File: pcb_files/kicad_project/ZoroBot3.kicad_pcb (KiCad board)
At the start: 2 copper layers, 85.8 x 91.9 mm, 197 parts, among them Q1 NMOS, Q2 AON7423, Q3 ST-1KL3A, Q4 ST-1KL3A, Q5 ST-1KL3A, Q6 ST-1KL3A, U1 MPU-6500, U2 MPU-6500, Y1 Crystal_GND24

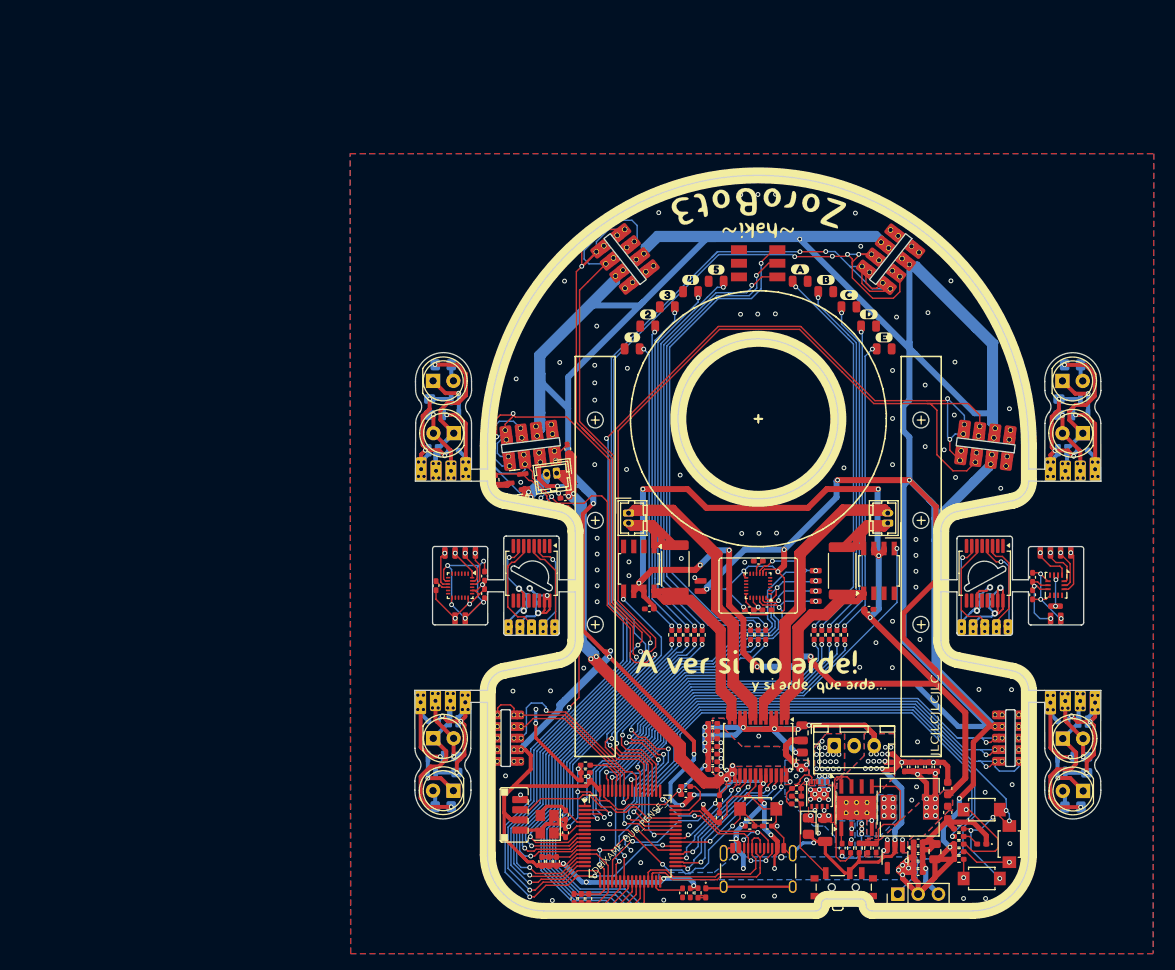
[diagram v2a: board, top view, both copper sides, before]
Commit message: Cambia el puente H al MP6551
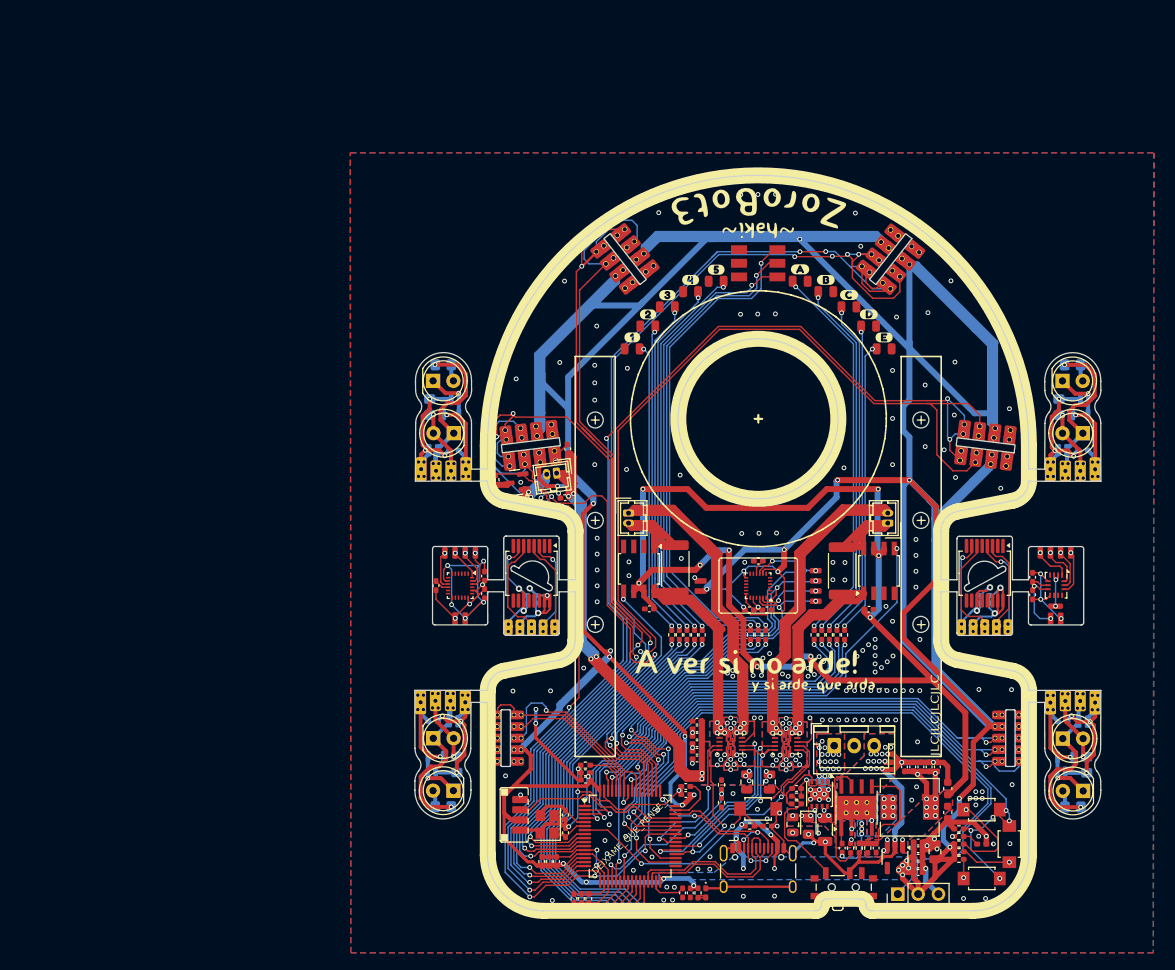
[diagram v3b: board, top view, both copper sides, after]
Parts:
- added PH2: ~, custom_footprints:PH-MP6551GQB-P, F.Cu at (147.1, 122.2)
- C43: footprint Capacitor_SMD:C_0402_1005Metric_Pad0.74x0.62mm_HandSolder -> Capacitor_SMD:C_0805_2012Metric
- PH1: footprint Package_SO:SSOP-24_5.3x8.2mm_P0.65mm -> custom_footprints:PH-MP6551GQB-P
- R12, R13: value 0.100 -> 0.05
- moved C5 8.18 mm to (154.9, 132.1), turned to 90 degrees
- moved C8 7.38 mm to (152.0, 126.8), turned to 90 degrees
- moved C43 6.88 mm to (149.2, 126.8), turned to 90 degrees
- moved PH1 3.48 mm to (154.1, 122.2), turned to 0 degrees
- moved C10 2.36 mm to (142.9, 123.9)
- moved C7 2.36 mm to (142.9, 122.0)
- moved C9 2.36 mm to (142.9, 122.9)
- moved C6 2.34 mm to (142.9, 121.0)
- moved C42 1.98 mm to (142.9, 120.1)
- moved C41 1.98 mm to (142.9, 119.2)
- moved R25 1.91 mm to (146.0, 127.1)
- moved R26 1.90 mm to (146.0, 129.3)
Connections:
- DEIXAME_QUE_PENSE_1 pad 33: /MOT_D_B -> unconnected-(DEIXAME_QUE_PENSE_1-PB12-Pad33)
- DEIXAME_QUE_PENSE_1 pad 34: /MOT_D_A -> /AUX_PIN
- DEIXAME_QUE_PENSE_1 pad 35: /MOT_I_B -> /LED_AUX
- DEIXAME_QUE_PENSE_1 pad 36: /MOT_I_A -> /MOT_ENABLE
- DEIXAME_QUE_PENSE_1 pad 37: /AUX_PIN -> /MOT_D_PWM_B
- DEIXAME_QUE_PENSE_1 pad 38: /MOT_S_PWM -> /MOT_D_PWM_A
- DEIXAME_QUE_PENSE_1 pad 39: /MOT_D_PWM -> /MOT_I_PWM_B
- DEIXAME_QUE_PENSE_1 pad 40: /MOT_I_PWM -> /MOT_I_PWM_A
- DEIXAME_QUE_PENSE_1 pad 41: /LED_AUX -> /MOT_S_PWM
- PH1 pad 1: /SHUNT_MD -> /MOT_D-
- PH1 pad 10: GND -> /MOT_D-
- PH1 pad 11: /SHUNT_MI -> unconnected-(PH1-CM2-Pad11)
- PH1 pad 12: /SHUNT_MI -> unconnected-(PH1-nFAULT-Pad12)
- PH1 pad 13: /BATT -> /MOT_D_PWM_B
- PH1 pad 14: /BATT -> /MOT_ENABLE
- PH1 pad 2: /SHUNT_MD -> /BATT
- PH1 pad 3: GND -> /SHUNT_MD
- PH1 pad 4: GND -> /MOT_ENABLE
- PH1 pad 5: /MOT_D- -> /MOT_D_PWM_A
- PH1 pad 6: /MOT_D- -> GND
- PH1 pad 7: /MOT_I+ -> unconnected-(PH1-CM1-Pad7)
- PH1 pad 8: /MOT_I+ -> /SHUNT_MD
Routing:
- net GND: track 289.1 -> 198.4 mm, vias 130 -> 203
- net /MOT_ENABLE: track 0.00 -> 53.0 mm, vias 0 -> 4
- net +3V3: track 804.2 -> 772.7 mm, vias 35 -> 33
- net /MOT_D_PWM_A: track 0.00 -> 25.0 mm, vias 0 -> 2
- net /MOT_D_PWM_B: track 0.00 -> 25.0 mm, vias 0 -> 2
- net /MOT_I_PWM_A: track 0.00 -> 20.2 mm, vias 0 -> 2
- net /MOT_D_A: track 19.4 -> 0.00 mm, vias 2 -> 0
- net /MOT_D_B: track 18.9 -> 0.00 mm, vias 2 -> 0
- net /MOT_I_PWM_B: track 0.00 -> 18.9 mm, vias 0 -> 2
- net /MOT_D_PWM: track 17.7 -> 0.00 mm, vias 2 -> 0
- net /MOT_I_A: track 14.8 -> 0.00 mm, vias 2 -> 0
- net /MOT_I_B: track 14.8 -> 0.00 mm, vias 2 -> 0
- net /SHUNT_MI: track 50.0 -> 64.5 mm, vias 0 -> 8
- net /MOT_I_PWM: track 12.3 -> 0.00 mm, vias 2 -> 0
- net /BATT: track 117.9 -> 107.8 mm, vias 34 -> 37
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- added copper zone on B.Cu, net /MOT_D-
- added copper zone on F.Cu, net /MOT_D-
- added copper zone on B.Cu, net /MOT_I+
- added copper zone on F.Cu, net /MOT_I+
- added copper zone on B.Cu, net /SHUNT_MD
- added copper zone on F.Cu, net /SHUNT_MD
- added copper zone on B.Cu, net /SHUNT_MI
- added copper zone on F.Cu, net /SHUNT_MI

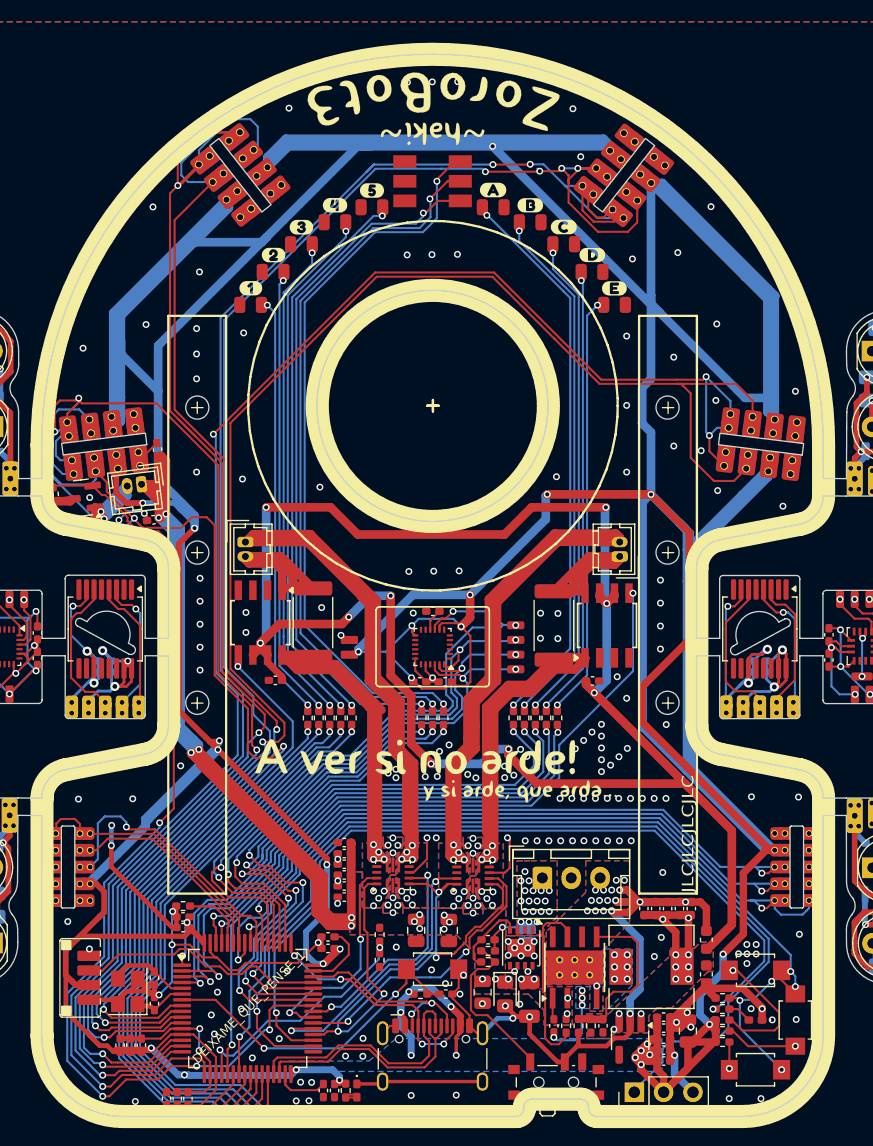
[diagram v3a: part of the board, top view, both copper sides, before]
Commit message: Desplaza ventilador y leds 2mm hacia adelante para hacer hueco a la bateria
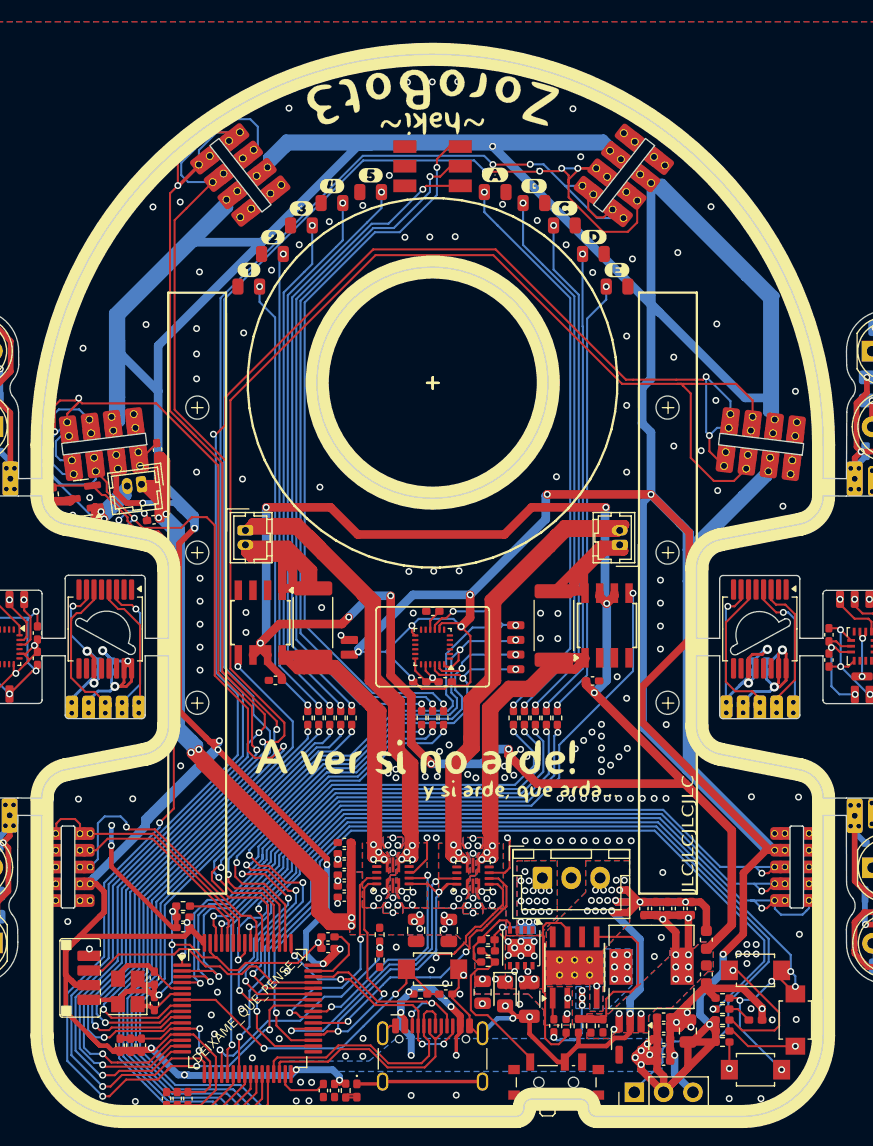
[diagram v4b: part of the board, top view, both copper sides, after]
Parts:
- moved kibuzzard-677A7C9A 1.69 mm to (159.4, 62.3)
- moved D7 1.69 mm to (159.4, 63.8)
- moved D4 1.68 mm to (141.9, 63.8)
- moved kibuzzard-677A7D86 1.68 mm to (141.9, 62.3)
- moved D8 1.62 mm to (162.0, 65.7)
- moved kibuzzard-677A7CA3 1.62 mm to (162.0, 64.3)
- moved D3 1.62 mm to (139.2, 65.7)
- moved kibuzzard-677A7D7B 1.62 mm to (139.2, 64.3)
- moved D10 1.60 mm to (166.6, 71.0)
- moved kibuzzard-677A7CBB 1.60 mm to (166.5, 69.6)
- moved D1 1.59 mm to (134.7, 71.0)
- moved kibuzzard-677A7E2E 1.59 mm to (134.7, 69.6)
- moved D9 1.56 mm to (164.5, 68.2)
- moved kibuzzard-677A7CAF 1.56 mm to (164.5, 66.7)
- moved D2 1.55 mm to (136.7, 68.2)
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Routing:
- net /MOT_I-: track 21.2 -> 28.3 mm
- net /EMI_PA_I: track 136.3 -> 130.8 mm
- net /MOT_D+: track 17.2 -> 20.6 mm
- net /EMI_FRONT_D: track 142.2 -> 145.2 mm
- net /SEN_FRONT_D: track 141.4 -> 144.1 mm
- net /MOT_D-: track 75.0 -> 77.4 mm
- net /MOT_I+: track 76.5 -> 78.7 mm
- net Net-(D3-A): track 43.1 -> 44.7 mm
- net Net-(D8-A): track 42.9 -> 44.5 mm
- net Net-(D4-A): track 46.3 -> 47.8 mm
- net Net-(D2-A): track 39.6 -> 41.1 mm
- net Net-(D7-A): track 46.1 -> 47.6 mm
- net Net-(D9-A): track 39.4 -> 40.9 mm
- net /SEN_PA_I: track 132.6 -> 134.0 mm
- net Net-(D10-A): track 37.1 -> 38.5 mm
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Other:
- outline, holes or cut-outs redrawn
